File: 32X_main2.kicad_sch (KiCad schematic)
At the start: 54 parts, among them IC501 SH2 M, IC502 SH2 S, IC503 µPD4502161, IC504 315-5818, IC506 315-5781, IC507 TC511664, IC508 TC511664, IC509 74AC04, IC510 RHSRL33A

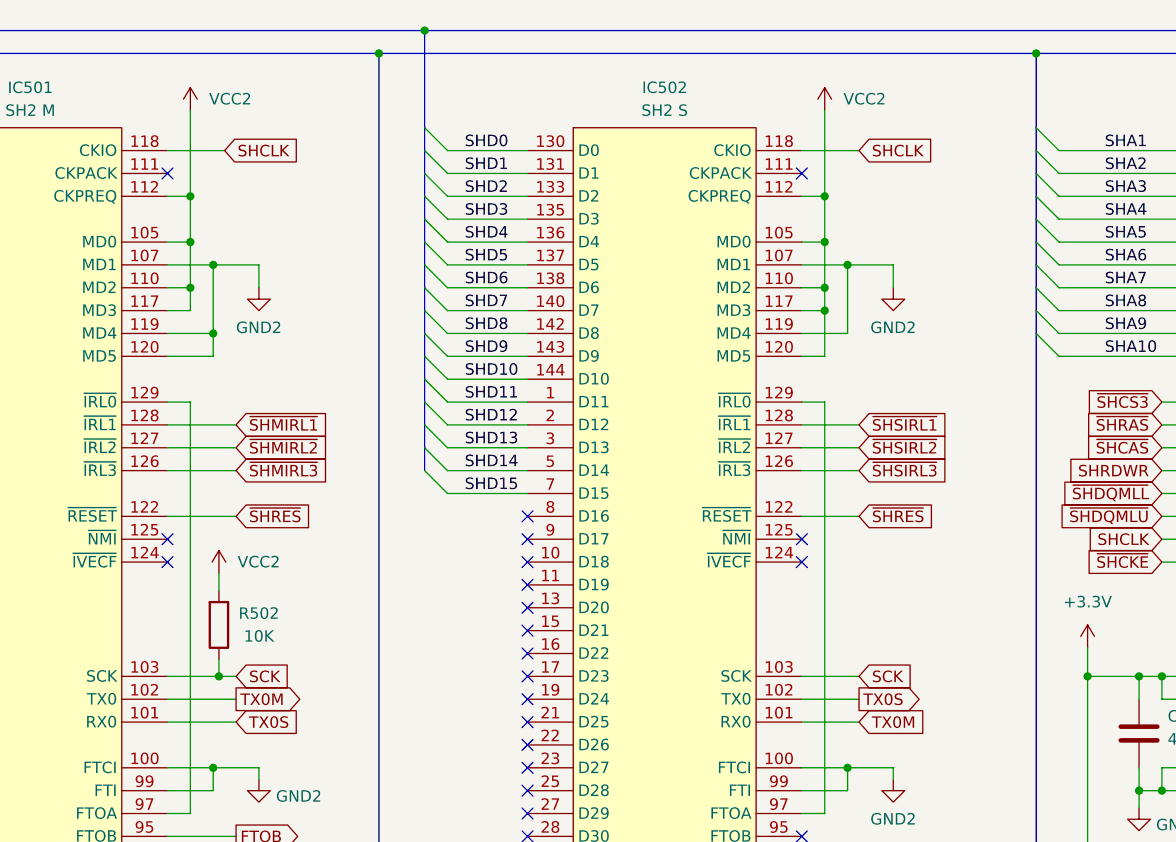
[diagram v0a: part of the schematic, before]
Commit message: Tie SH2 NMI pins to VCC as per original 32X main board (not obvious from schematic).
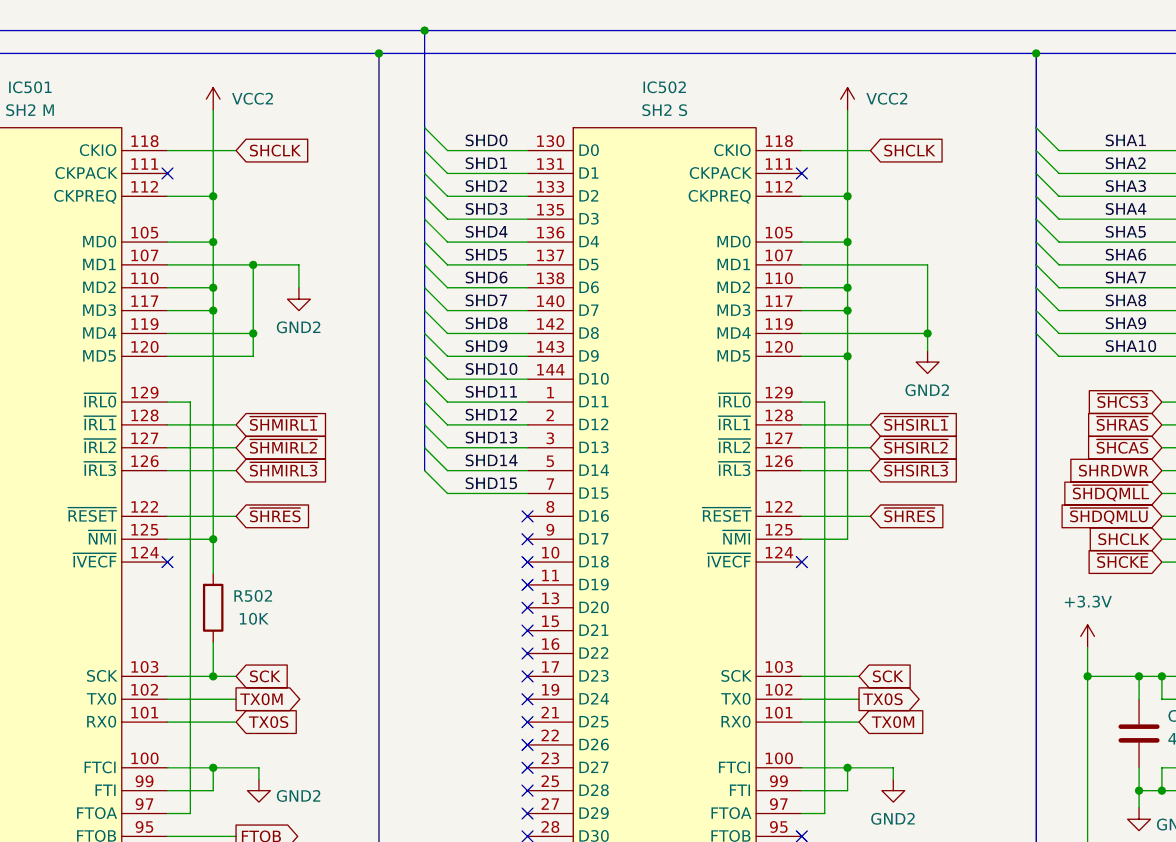
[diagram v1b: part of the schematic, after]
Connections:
- net VCC2: now also IC501.125 (~{NMI}), IC502.125 (~{NMI})
- no-connect marks 70 -> 68
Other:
- moved on the sheet: R502
